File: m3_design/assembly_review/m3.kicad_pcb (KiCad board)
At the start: 4 copper layers, 46 x 90 mm, 245 parts, among them J1 DB125-3.5-2P-GN-S, J121 DB125-3.5-2P-BK-S, J122 SERVO 3x4, J123 BM02B-GHS-TBT(LF)(SN), J124 DB125-3.5-2P-BK-S, J2 TC2030-IDC-NL SWD, J3 USB-C 2.0, J400 BM02B-GHS-TBT(LF)(SN), J410 GPS 4V8/GND/TX/RX, J420 RADIO 4V8/GND/TX/RX, J9 CAMERA 5V/GND/RX/TX, Q120 AON6403, Q121 AON6403, Q122 AO3400A, Q123 AO3400A, Q124 AON7524, U1 STM32H743VIT6, U10 TPS2553DBVR, U11 TPS2121RUXR, U12 TXU0202DCUR, U13 TPS70933DBVR, U2 AP63203WU-7, U3 W25Q128JVSIQ, U4 LSM6DSV320X, U400 AP63201WU-7, U401 TPS7A9101DSKR, U402 TPS2553DBVR, U410 TPS2553DBVR, U411 TXU0202DCUR, U412 TPS70933DBVR, U420 TPS2553DBVR, U421 TXU0202DCUR, U422 TPS70933DBVR, U5 MS561101BA03, U9 TPS259470LRPWR, Y1 25MHz CL8pF

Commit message: R10 owner answers implemented (OQ-1/2/4/5/6/7); single-switch and audit-cut decisions recorded
OQ-2 hot-plug re-modelled on R10's extracted feed (tools/r10_hotplug.py, hotplug.md), damper R166 0.36 ohm
(C168925), F9-1 retargeted to the model; OQ-1 P-11 floor 4.95 mm; OQ-5 firmware load shedding, no hardware cutoff;
OQ-6 no battery-lead fuse (J1 fuse legend removed); OQ-7 board forward of joint +47 mm; OQ-4 aft-edge tab and panel
rail in ORDERING. R10_DECISIONS: requirements-audit cuts AUD-1..10 / GAP-1..5 and the owner's single screw switch
decision (to be implemented next). Board b860afbe..., 46 x 90 mm; two rebuilds byte-identical (agent);
tools/check.sh exit 0 (DRC 0, R10 CAD contract OK, routing hygiene OK, actuator safety contract OK, fab manifest OK).

Co-Authored-By: Claude Opus 5.5 <noreply@anthropic.com>
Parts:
- R166: value 0.33R 1% 2512 -> 0.36R 1% 2512
- R92: value 10k 1% -> 3.3k 1%
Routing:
- net BAT_IN: track 88.4 -> 92.4 mm, vias 1 -> 2
- net BAT_DAMP: track 10.4 -> 12.2 mm
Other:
- board text removed: "J1 BAT 15A FUSE"

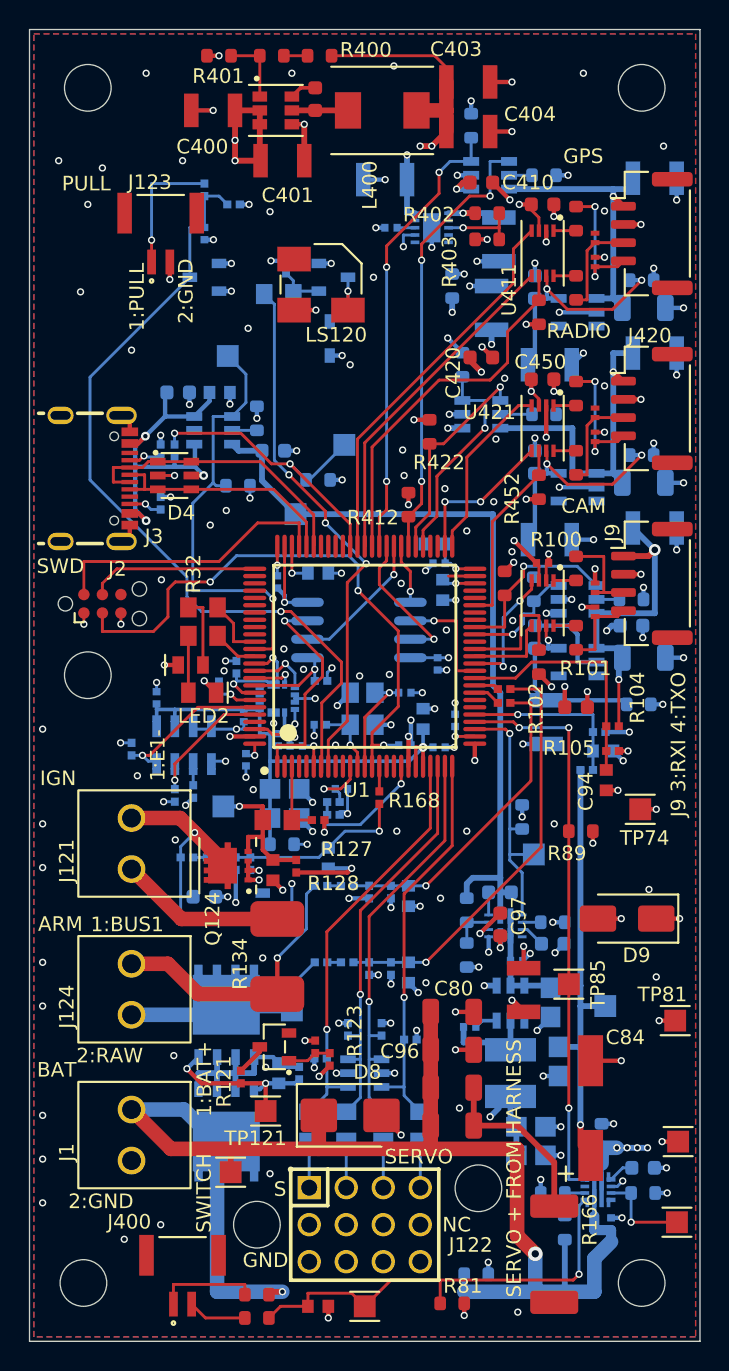
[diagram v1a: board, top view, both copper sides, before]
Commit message: R10 single screw-switch arming pass before review round 9
Preparatory single-switch pass, not a full review round or clean-round credit.
Remove J124 and its fused ARM link, join the post-switch bus as RAW_ACT, and
implement the independent PC1 load-switch enable through R122/Q122 while PE4
controls the fire FET. Move R134 for direct bottom-side fire routing. Update
schematic/PCB generators, contracts, seeded tests, binding and operating records.
No interrupted changes were discarded. AUD/GAP cuts and fresh round 9 follow.

Board SHA-256: 60be35eaff86dd7a5fb8e065aa4204a51e7d786d7dfc8d2456cdd66c4b86f901
Board: 46 x 90 mm, 4 layers, 2521622 bytes. Two full builds are byte-identical.
Netlist SHA-256: 3e08722d7ac997131cb11d7c9cb2d25e1b3babcfb853b71230db01118bc70e69
Fab: 228 CPL rows, 83 BOM lines; orientation, paste and manifest checks pass.
Hot-plug: same input-feed signature; 2304 corners and local sensitivities pass
(simulation / Inference). Bench, firmware, RF immunity and physical fit unverified.

Final unskipped tools/check.sh: exit 0
DRC violations 0  unconnected 0  schematic parity 0  ERC 0
metadata / 3D model audit: OK
fit check: OK (CAD envelopes only)
R10 CAD contract (full): OK
routing hygiene: 0 failing, 0 allowlisted, 0 leftovers recorded
actuator safety contract: OK
Fab manifest: OK; 5 outputs match the current CAD and export inputs
Self-tests: shell 4, fit 23, paste 5, route 57; R10 122 (3 NumPy tests
skipped in KiCad Python then passed separately). Standalone plate 3 passed.
Added local absolute paths: 0. No direct Git index/commit mutation performed.

Co-Authored-By: Claude Opus 5.5 <noreply@anthropic.com>
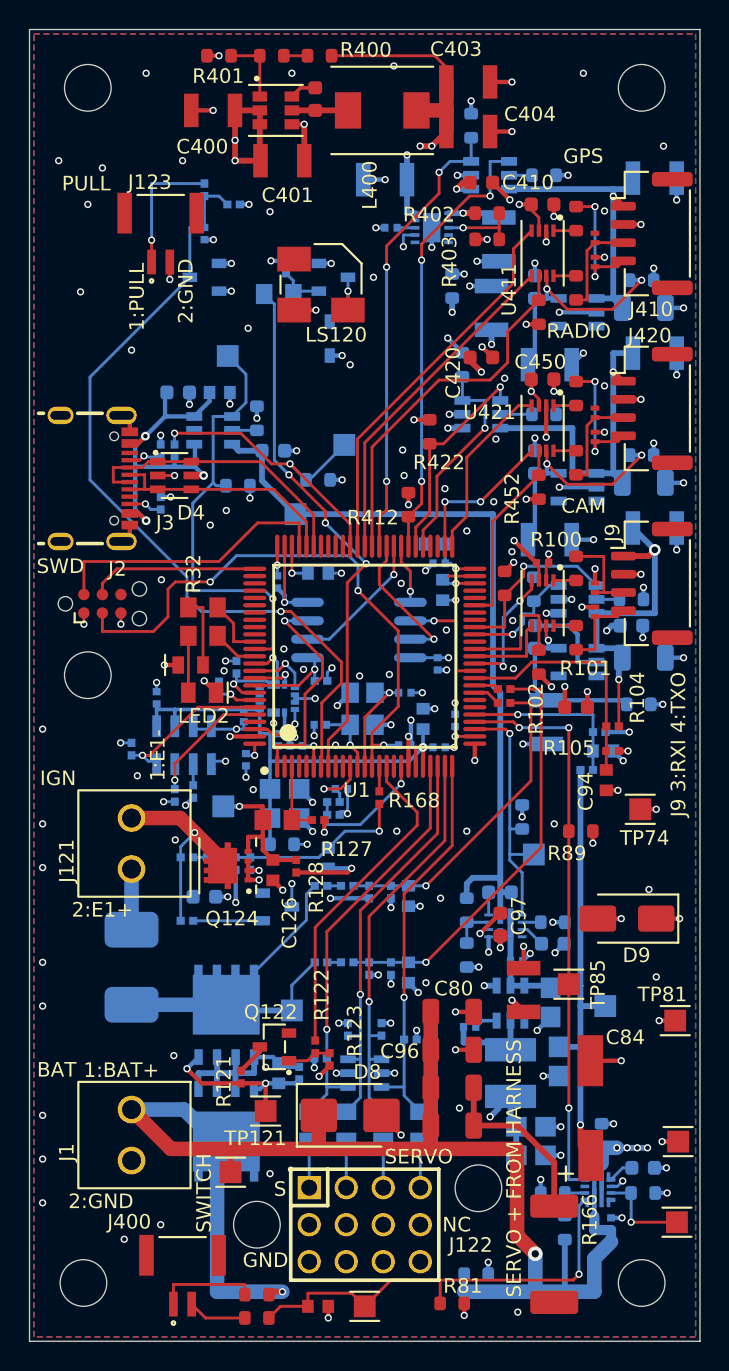
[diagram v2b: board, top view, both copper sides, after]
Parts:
- removed J124: DB125-3.5-2P-BK-S, rocket:M3_DB125_2P_BK
- R122: value 100k -> 1k
- R134: moved to B.Cu
- moved R134 10.0 mm to (7.00, 64.3)
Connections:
- R122 pad 1: RAW_PROTECTED -> ACT_EN_MCU
- R132 pad 1: PYRO1_BUS -> RAW_ACT
- R134 pad 2: PYRO1_BUS -> RAW_ACT
- U1 pad 16: unconnected-(U1-PC1-Pad16) -> ACT_EN_MCU
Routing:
- net ACT_EN_MCU: track 0.00 -> 22.6 mm
- net PYRO1_BUS: track 19.3 -> 0.00 mm, vias 1 -> 0
- net RAW_ACT: track 11.1 -> 20.7 mm
- net PYRO1_IGN: track 11.4 -> 4.16 mm
- net GND: track 186.8 -> 188.1 mm, vias 211 -> 210
- net RAW_PROTECTED: track 22.6 -> 21.9 mm, vias 11 -> 10
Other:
- board text removed: "1:BUS1"
- board text removed: "2:RAW"
- board text removed: "ARM"
- board text removed: "J124 5A FAST 2S"
- board text removed: "J124 ARM LAST"

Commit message: R10 requirements-audit cuts and GAP fixes before review round 9
Implement adopted AUD-1 through AUD-10 and GAP-1 through GAP-5 after the single-switch pass.
Remove the advisory pull-pin, redundant probes and GPS/radio IO LDO cells; qualify the smaller
AONR21357 pair, correct C120 voltage rating, standardize shared-code capacitor lands, simplify
slow returns and fire-only copper, localize U9 output protection and add exactly two U401 VIPPO vias.
Record physical-current timing, coupled fire/source budget, C84 manual fitting and narrowed gate scopes.

Board SHA-256: 877d01996a59e9dd5c6dbc367274bb9a323a13982d67960fe46df9b0ee53205d
Board: 46 x 90 mm, 4 layers, 2365477 bytes; 225 footprints, 883 straight tracks, 323 vias.
Netlist SHA-256: 0843da709e2d7a757e9b35cdff48158a54012c5353619cbf409ab961efd2c3ca
Two fresh complete passing builds are byte-identical. Schematic: 700 pins; 22 seeded faults detected.

Final unskipped tools/check.sh: exit 0
DRC violations 0  unconnected 0  schematic parity 0  ERC 0
metadata / 3D model audit: OK
silkscreen outside the board outline: 0 stroke points
fit check: OK (CAD envelopes only)
R10 CAD contract (full): OK
routing hygiene: 0 failing, 0 allowlisted, 0 leftovers recorded
actuator safety contract: OK
Fab manifest: OK; 5 outputs match current CAD and export inputs
Self-tests: shell 4, fit 24, paste 5, routing 59, R10 131; three NumPy cases rerun and passed.

Fab: 215 CPL rows, 82 BOM codes; orientation / paste / manifest pass. Hot-plug: 2304 required
cases plus convergence and controls pass (simulation / Inference). Plate f1 280.9 Hz (Inference).
Live JLC: $84.43 vs $84.41 target, 46 Extended codes; R430 / U4 short. Procurement exit 1 is a
disclosed OQ-3 / ordering deviation, not a CAD gate pass. No quote accepted or order placed.
Firmware, bench, thermal/transient correlation, process acceptance, installed RF immunity and physical fit unverified.

This preparatory pass earns no clean-review credit. Start fresh full ten-lens round 9 on th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
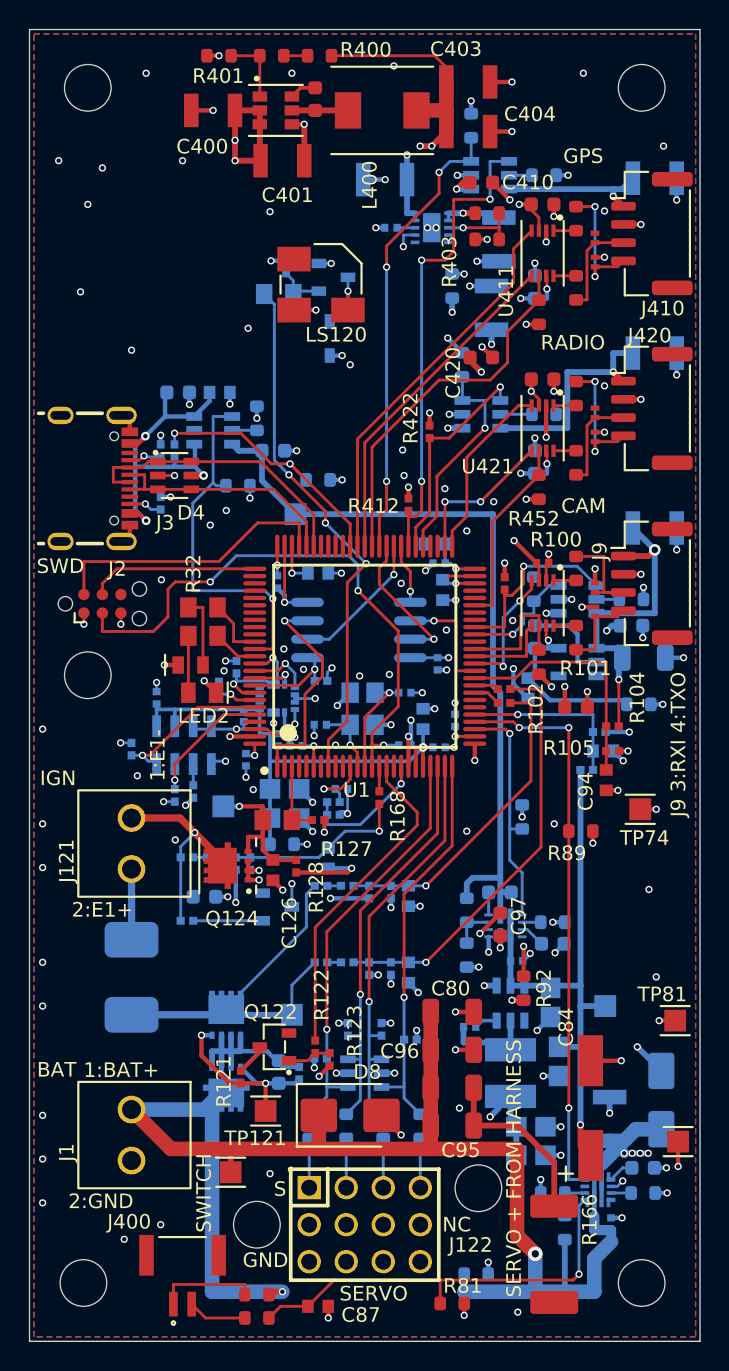
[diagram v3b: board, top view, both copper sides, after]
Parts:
- removed C160: 100nF 50V X7R 10%, rocket:C0402
- removed C441, C451: 1uF 50V X7R 10%, rocket:C_1206_3216Metric
- removed C442, C452: 22uF 25V X7R 10%, rocket:M3_GRM32_1210
- removed D122: BAT54S, rocket:SOT-23-3_L2.9-W1.3-P1.90-LS2.4-BR
- removed J123: BM02B-GHS-TBT(LF)(SN), rocket:M3_GH_BM02B_GHS_TBT
- removed R160: 1k, rocket:R0402
- removed R161: 10k, rocket:R0402
- removed R443, R453: 1k 1%, rocket:R_0603_1608Metric
- removed TP84: BAT_ENABLE, rocket:M3_TestPad_1.5
- removed TP85: BAT_FAULT_N, rocket:M3_TestPad_1.5
- removed TP86: USB_FAULT_N, rocket:M3_TestPad_1.5
- removed TP87: LOGIC_SOURCE_ST, rocket:M3_TestPad_1.5
- removed TP89: BAT_ILIM, rocket:M3_TestPad_1.5
- removed TP92: VBUS_SENSE, rocket:M3_TestPad_1.5
- removed U412, U422: TPS70933DBVR, rocket:M3_TPS709_DBV
- C120: value 2.2uF -> 1uF 25V X7R 10%; footprint rocket:C0603 -> rocket:C_0603_1608Metric
- C82, D9: moved to B.Cu
- C92: value 22uF 25V X7R 10% -> 4.7uF 16V X5R 10%; footprint rocket:M3_GRM32_1210 -> rocket:C0603
- Q120, Q121: value AON6403 -> AONR21357; footprint rocket:PDFN-8_L5.6-W5.2-P1.27-LS6.1-BL -> rocket:M3_AONR21357_DFN3x3A_EP1
- R150, R151, R152, R153: value 1k 0805 -> 1k 0603; footprint rocket:R0805 -> rocket:R_0603_1608Metric
- R412, R422, R432: value 10k 0.1% -> 10k 1%; footprint rocket:R_0603_1608Metric -> rocket:R0402
- R92: moved to F.Cu
- moved D9 12.7 mm to (43.4, 73.5), turned to 90 degrees
- moved R92 11.5 mm to (33.9, 65.8)
- moved C82 10.6 mm to (39.8, 74.8)
- moved Q120 3.00 mm to (13.5, 72.6)
- moved C92 2.64 mm to (34.2, 45.2)
- moved R134 0.69 mm to (7.00, 65.0)
- moved TP120 0.30 mm to (18.0, 67.6)
- moved C120 0.07 mm to (17.1, 71.5)
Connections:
- C443 pad 1: GPS_IO_3V3 -> 3V3
- C453 pad 1: RADIO_IO_3V3 -> 3V3
- U1 pad 7: PULLPIN -> unconnected-(U1-PC13-Pad7)
- U411 pad 7: GPS_IO_3V3 -> 3V3
- U421 pad 7: RADIO_IO_3V3 -> 3V3
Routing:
- net PULLPIN: track 56.5 -> 0.00 mm, vias 1 -> 0
- net RADIO_IO_3V3: track 16.7 -> 0.00 mm, vias 2 -> 0
- net GPS_IO_3V3: track 16.7 -> 0.00 mm, vias 2 -> 0
- net GND: track 188.1 -> 175.2 mm, vias 210 -> 190
- net PULLPIN_EXT: track 9.00 -> 0.00 mm, vias 1 -> 0
- net GPS_4V8: track 19.0 -> 10.3 mm
- net RADIO_4V8: track 22.2 -> 15.1 mm
- net BAT_IN: track 92.4 -> 98.7 mm
- net BAT_ILIM: track 6.52 -> 1.38 mm, vias 1 -> 0
- net USB_FAULT_N: track 30.3 -> 25.2 mm
- net 3V3: track 50.4 -> 55.5 mm, vias 31 -> 33
- net RAW_ACT: track 20.7 -> 24.7 mm
- net VBUS_SENSE: track 22.2 -> 18.5 mm
- net GPS_FAULT_N: track 30.8 -> 33.1 mm
- net RAW_PROTECTED: track 21.9 -> 23.8 mm, vias 10 -> 9
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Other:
- board text added: "J410 1:4V8"
- board text added: "J410 2:GND"
- board text added: "J410 3:TXO"
- board text added: "J410 4:RXI"
- board text added: "J420 1:4V8"
- board text added: "J420 2:GND"
- board text added: "J420 3:TXO"
- board text added: "J420 4:RXI"
- board text removed: "1:PULL"
- board text removed: "PULL"

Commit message: Finish R10 round 9 Minor fix pass
Complete the interrupted generator rebuild and apply the recorded round 9
Minor fixes: capacitor labels, cold-screen ordering, debugger instructions,
local route cleanups, gate fault detection and explicit R10 procurement limits.
Refresh the board-bound fabrication, supplier and validation records.

Round 9 reviewed 8bccb07: 0 Critical, 0 Major, 21 Minor groups. Round 10 will
freshly review this committed fix pass, including every changed CAD item.

Board SHA-256: b337fe63c258c85ba4120e75ad018afa0c22241f8bc21a4172787cf2887208d9
Board: 46 x 90 mm, 2366509 bytes. Two COMPLETE builds pass; all 21 generated
CAD and binding files are byte-identical.

Unskipped tools/check.sh: exit 0.
DRC violations 0; unconnected 0; schematic parity 0; ERC 0.
Metadata / 3D, silk, fit / plate, all 33 R10 rules, routing hygiene, actuator
contract and current 5-output fabrication manifest: OK.
Self-tests: shell 4, procurement 19, fit 24, paste 5, routing 59, R10 140;
3 NumPy cases rerun successfully, no unresolved skips. Hot-plug: 2304/2304
required cases pass (simulation / Inference).

Fab export, required fitting, orientation and paste pass: 215 CPL rows,
82 BOM codes. Fresh supplier/procurement checks correctly FAIL the known
$84.43 versus $84.41 cap and R430/U4 stock shortages; 46 Extended codes.
OQ-3 and final deviation acceptance remain pending. No firmware, bench,
installed RF immunity, physical fit, assembly-process or flight result claimed.

Evidence: docs/R10_VALIDATION.md and sources/r10_review/round9_fix_validation.json
and round9_fix_check.txt under m3_design/assembly_review. Native headless
KiCad environment uses the external D-R1-05 mouse-query workaround only;
repository gates and CAD rules are unchanged by that workaround.

Co-Authored-By: Claude Opus 5.5 <noreply@anthropic.com>
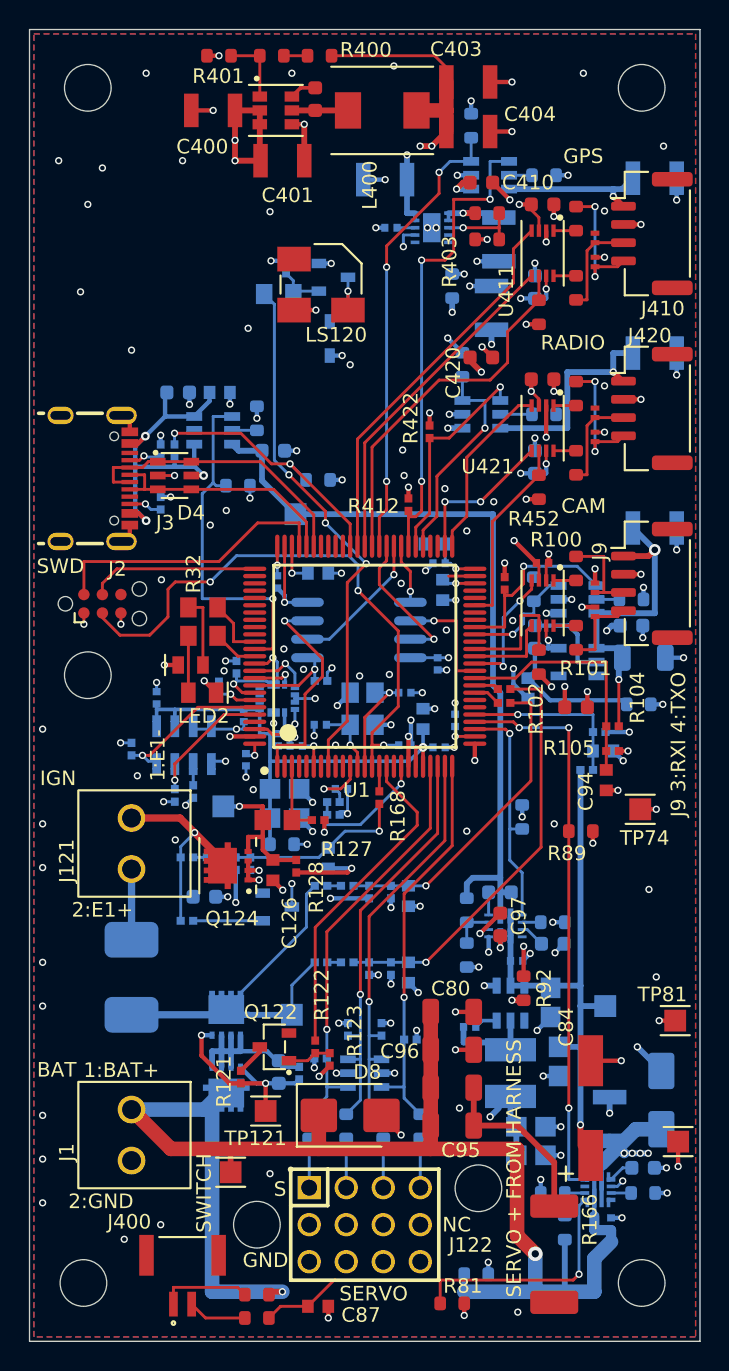
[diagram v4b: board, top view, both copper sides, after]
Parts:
- C10, C11, C6, C7, C8, C9: value 22uF -> 22uF 25V X5R 20%
- C122, C127, C129, C60, C94: value 10nF -> 10nF 50V X7R 10%
- C19, C20, C87: value 2.2uF -> 2.2uF 16V X5R 10%
- C22: value 1uF -> 1uF 50V X5R 10%
- C23, C28: value 4.7uF -> 4.7uF 16V X5R 10%
- C25, C26: value 10pF -> 10pF 50V C0G 5%
- C88, C99: value 100nF 50V -> 100nF 50V X7R 10%
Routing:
- net BAT_SW_SOURCE: track 6.95 -> 6.26 mm
- net USB_FAULT_N: track 25.2 -> 24.6 mm
